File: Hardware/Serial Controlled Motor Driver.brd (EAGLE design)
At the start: 25.4 x 25.4 mm, 43 parts, among them J1 DNP, J2 DNP, J3 DNP, J4 DNP, J5 DNP, J6 DNP, J7 DNP, U1 CY8C4245LQI-483, U2 DRV8835

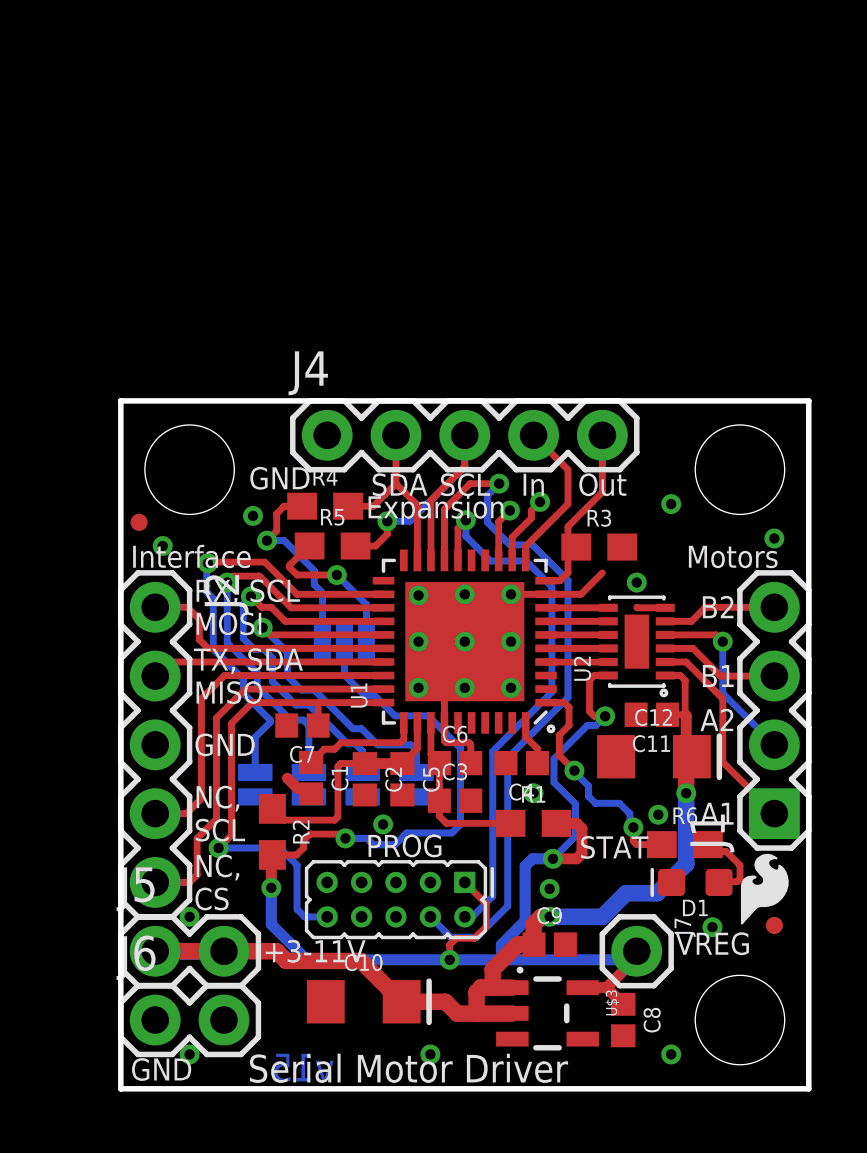
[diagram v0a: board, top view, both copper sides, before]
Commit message: Prepping for QC, tuning gitignores
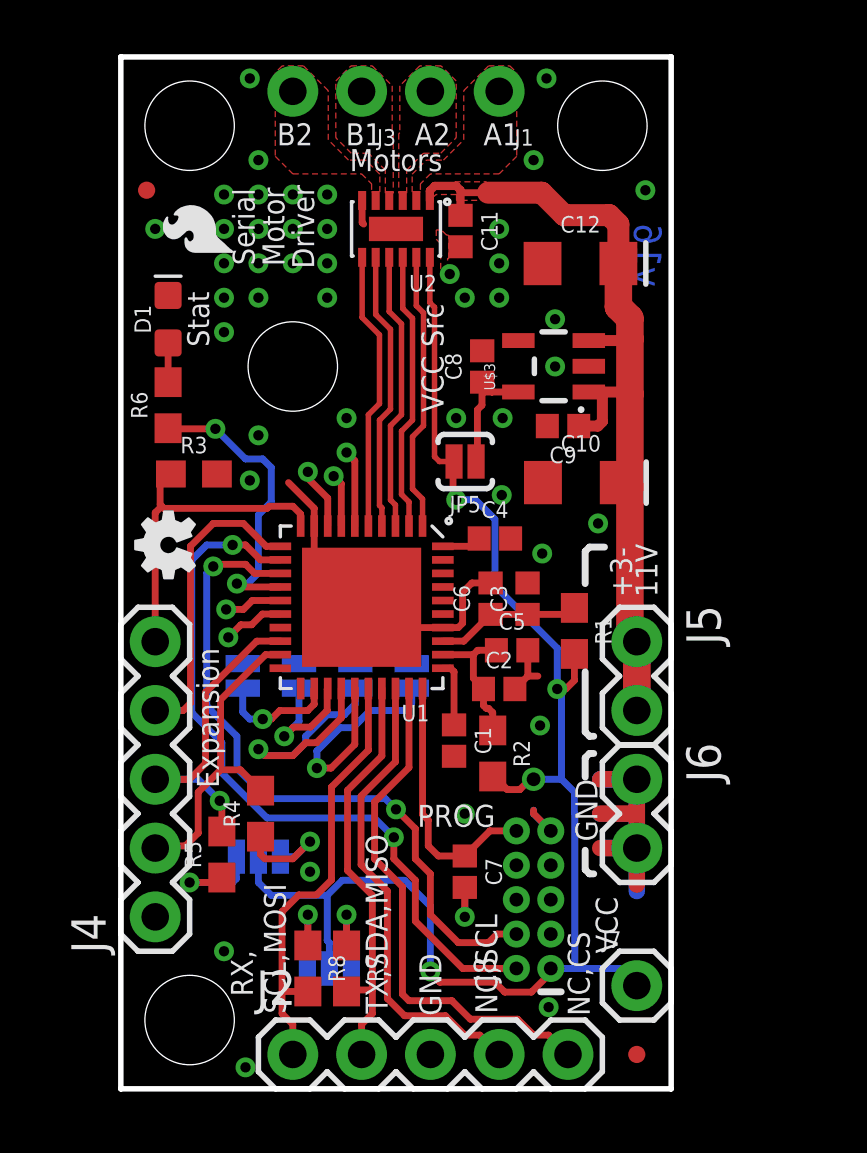
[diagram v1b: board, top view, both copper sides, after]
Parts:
- added H4: STAND-OFF, SparkFun-Electromechanical:STAND-OFF
- added J8: CORTEX_DEBUGPTH, Pete_Connectors_Retired:2X5-PTH-1.27MM
- added JP6, JP7: JUMPER-PAD-3-NOYES_SILK, SparkFun-Passives:PAD-JUMPER-3-NO_YES_SILK
- added R7, R8: 4.7k, SparkFun-Resistors:0603
- J1: device SparkFun-Connectors:1X04 -> SparkFun-Connectors:1X02_NO_SILK
- J3: device SparkFun-Connectors:2X5_PTH_SILK_.05 -> SparkFun-Connectors:1X02_NO_SILK
- J5, J6: device SparkFun-Connectors:1X02 -> SparkFun-Connectors:1X02@1
- JP5: value JUMPER-PAD-3-NOYES_SILK -> JUMPER-PAD-2; device SparkFun-Passives:PAD-JUMPER-3-NO_YES_SILK -> SparkFun-Jumpers:PAD-JUMPER-2-NC_BY_PASTE_YES_SILK
- moved H2 38.8 mm to (2.54, 35.6)
- moved FD2 35.7 mm to (0.95, 33.2), turned to 90 degrees
- moved LOGO1 30.8 mm to (4.48, 30.6), turned to 90 degrees
- moved J3 29.3 mm to (8.89, 36.8), turned to 180 degrees
- moved J1 28.5 mm to (14.0, 36.8), turned to 180 degrees
- moved D1 28.5 mm to (1.75, 28.4)
- moved FD1 26.9 mm to (19.1, 1.27), turned to 90 degrees
- moved LOGO2 25.4 mm to (1.75, 20.1), flipped to the top, turned to 90 degrees
- moved R6 25.0 mm to (1.75, 25.2), turned to 90 degrees
- moved C8 24.7 mm to (13.3, 26.7), turned to 90 degrees
- moved U$3 23.9 mm to (16.0, 26.7), turned to 90 degrees
- moved J5 21.1 mm to (19.1, 16.5), turned to 270 degrees
- moved C10 20.8 mm to (17.0, 22.4)
- moved J6 19.9 mm to (19.1, 11.4), turned to 270 degrees
- moved C11 19.2 mm to (12.5, 31.7), turned to 270 degrees
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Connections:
- net N$5 renamed AOUT1
- net P3.5_US renamed U3.5
- removed net N$7: J1.4, U2.5
- removed net N$8: J1.3, U2.3
- removed net N$9: JP5.3, R4.1
- removed net P2.5: U1.6, U2.9
- removed net P2.6: U1.7, U2.8
- removed net P2.7: U1.8, U2.7
- removed net P3.4_US: U1.14
- removed net P3.6: J3.2, U1.16
- removed net P3.7: J3.4, U1.17
- removed net TEST1: U1.12
- removed net TEST2: U1.13
- new net AOUT2: J1.2, U2.3
- new net BOUT1: J3.1, U2.4
- new net BOUT2: J3.2, U2.5
- new net N$11: JP6.1, R8.1
- new net N$12: JP6.3, R7.1
- new net N$5: C8.1, JP5.1, U$3.5
- new net P2.1: U1.2, U2.10
- new net P2.2: U1.3, U2.9
- new net P3.2: J8.2, U1.12
- new net P3.3: J8.4, U1.13
- new net SLED: R6.1, U1.14
- new net U2.5: U1.6
- new net U2.6: U1.7
- new net U2.7: U1.8
- new net U3.6: U1.16
- net !RESET: now also J8.10; no longer J3.10
- net GND: now also J8.3, J8.5, J8.7, J8.9, U$3.2; no longer J3.3, J3.5, J3.7, J3.9, U$3.3
- net N$2: now also JP7.1, R4.1; no longer JP5.1, R5.1
- net N$6: now also JP7.3, R5.1; no longer J1.2, U2.4
- net P2.0: now also U2.11; no longer R6.1
- net P2.3: now also U2.8; no longer U2.11
- net P2.4: now also U2.7; no longer U2.10
- net RX_SCL_MOSI_IN: now also R8.2
- net TX_SDA_MISO_IN: now also R7.2
- net VCC: now also J8.1, JP6.2, JP7.2; no longer C8.1, J3.1, U$3.5
- net VIN: now also U$3.3; no longer U$3.2
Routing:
- net P3.2: track 0.00 -> 27.3 mm, vias 0 -> 2
- net P3.7: track 26.4 -> 0.00 mm, vias 1 -> 0
- net P3.3: track 0.00 -> 25.3 mm, vias 0 -> 2
- net P3.6: track 19.8 -> 0.00 mm, vias 1 -> 0
- net GND: track 14.0 -> 33.5 mm, vias 23 -> 44
- net MODEB0: track 15.9 -> 4.44 mm
- net SLED: track 0.00 -> 11.1 mm, vias 0 -> 2
- net P2.2: track 0.00 -> 10.4 mm
- net P2.1: track 0.00 -> 10.4 mm
- net MODEB1: track 14.9 -> 4.81 mm
- net P2.4: track 2.30 -> 10.4 mm
- net P2.3: track 2.30 -> 10.4 mm
- net !RESET: track 17.6 -> 9.69 mm, vias 1 -> 0
- net AOUT1: track 7.72 -> 0.00 mm
- net N$9: track 7.14 -> 0.00 mm, vias 1 -> 0
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- added copper zone on layer 1, net AOUT1
- added copper zone on layer 1, net AOUT2
- added copper zone on layer 1, net BOUT1
- added copper zone on layer 1, net BOUT2
- added copper zone on layer 1, net VIN
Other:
- board size 25.4 x 25.4 mm -> 20.3 x 38.1 mm
- board text added: "(Open=UART)"
- board text added: "+3- 11V"
- board text added: "A"
- board text added: "B"
- board text added: "Exp. PU"
- board text added: "NC,CS"
- board text added: "NC,SCL"
- board text added: "RX, SCL,MOSI"
- board text added: "Stat"
- board text added: "TX,SDA,MISO"
- board text added: "These lines depict the width of typical TO-220 heatsinks."
- board text added: "User PU"
- board text added: "VCC"
- board text added: "VCC Src"
- board text added: "v16"
- board text removed: "(bridge='1')"
- board text removed: "+"
- board text removed: "+3-11V"
- board text removed: "0000:UART 0001:SPI 0010:SLV 0011:0x58 0100:0x59 (...)"
- board text removed: "Interface"
- board text removed: "NC, CS"
- board text removed: "NC, SCL"
- board text removed: "Pull Enb"
- board text removed: "RX, SCL MOSI"
- board text removed: "STAT"
- board text removed: "TX, SDA MISO"
- board text removed: "VREG"
- board text removed: "v15"
